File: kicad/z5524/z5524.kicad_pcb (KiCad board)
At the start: 4 copper layers, 80 x 80 mm, 203 parts, among them J1 Conn_01x01, J2 Conn_01x02, J3 Conn_02x20_Odd_Even, Q1 2N7002K, U1 TL074, U10 TL072, U11 NE5532, U12 TL074, U13 AS3364, U14 AD5328, U15 M24C02-WMN, U16 SSI2130, U17 DG442xY, U18 TL072, U19 LM311, U2 LM337L_TO92, U21 AD5328, U3 LM4040BIM3-2.5, U4 LM4040BIM3-4.1, U5 DG442xY, U6 TL072, U7 PCA9555D, U8 LM78L05_TO92, U9 AS3394

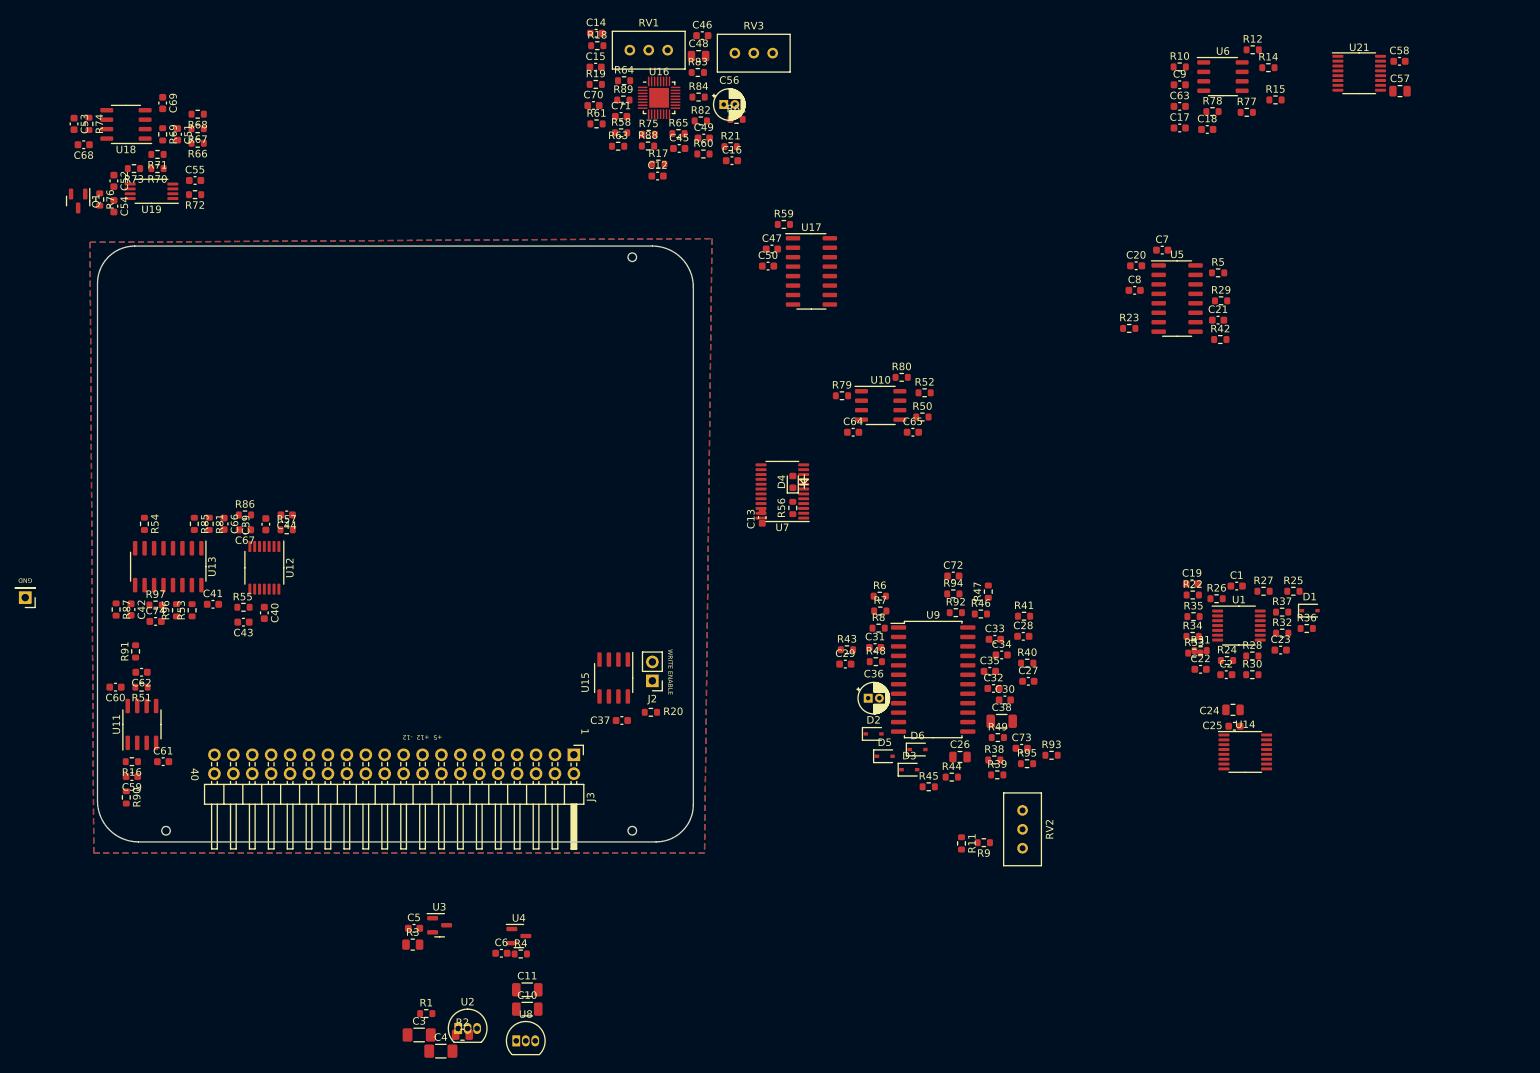
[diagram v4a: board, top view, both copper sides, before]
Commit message: further footprint mods; some placement
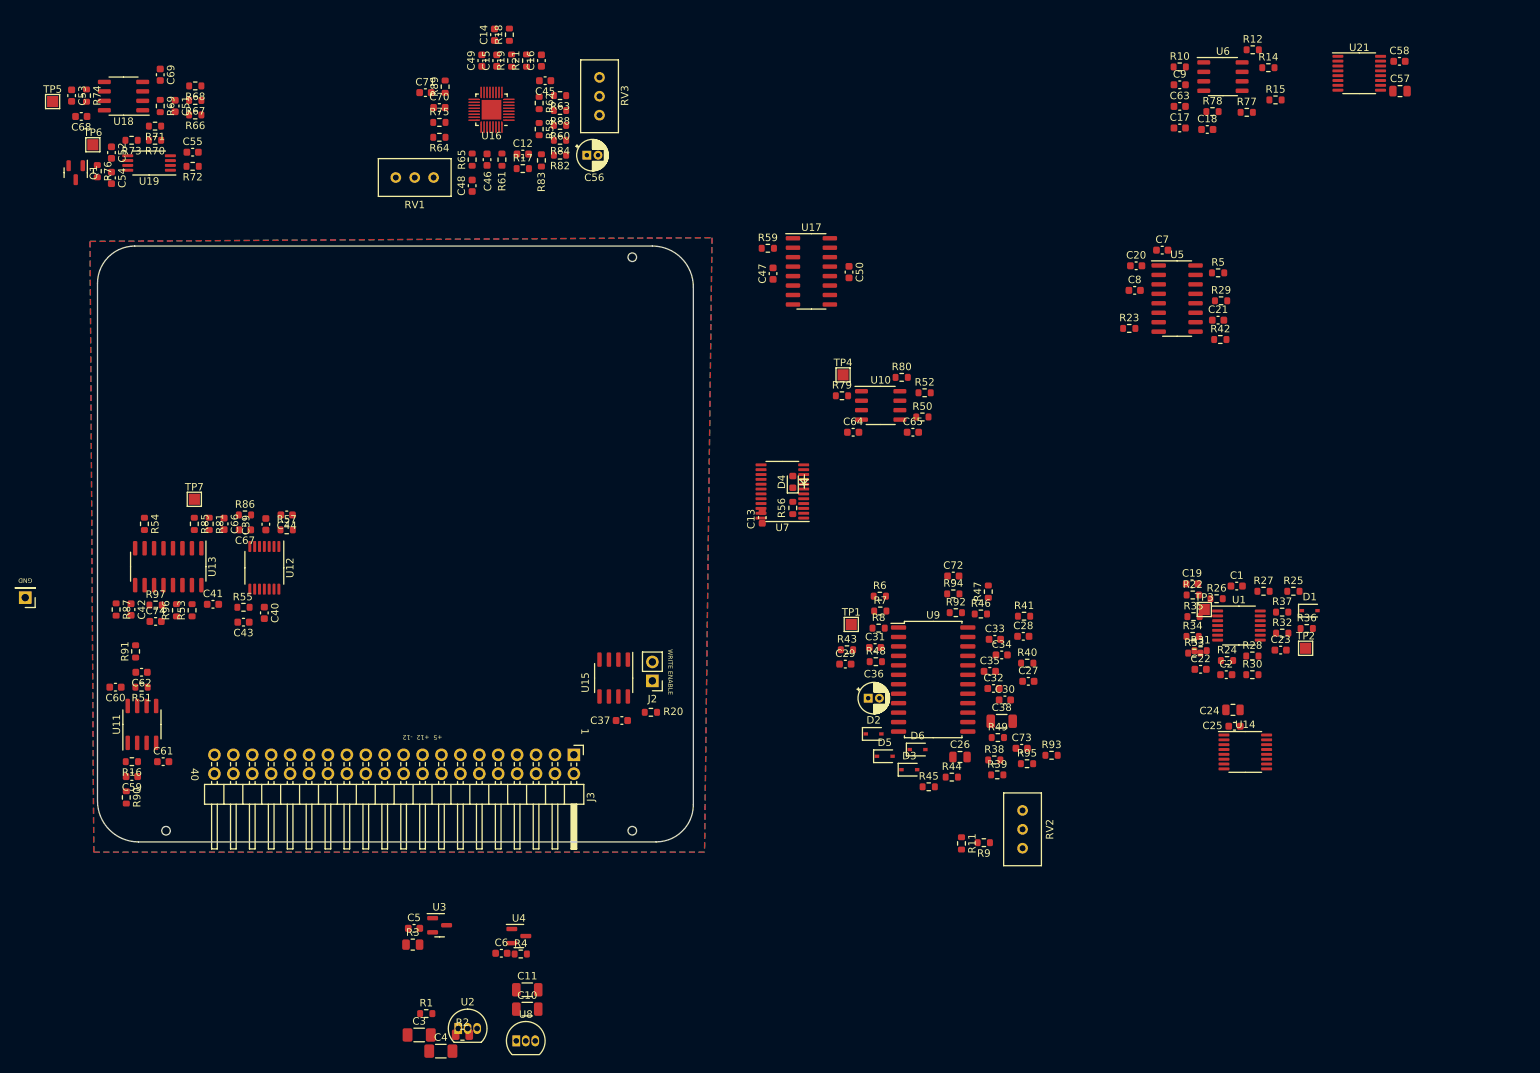
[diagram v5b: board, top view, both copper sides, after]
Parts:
- added TP1: TestPoint, TestPoint:TestPoint_Pad_1.5x1.5mm, F.Cu at (166.6, 75.7)
- added TP2: TestPoint, TestPoint:TestPoint_Pad_1.5x1.5mm, F.Cu at (227.6, 78.9)
- added TP3: TestPoint, TestPoint:TestPoint_Pad_1.5x1.5mm, F.Cu at (214.0, 73.7)
- added TP4: TestPoint, TestPoint:TestPoint_Pad_1.5x1.5mm, F.Cu at (165.5, 42.2)
- added TP5: TestPoint, TestPoint:TestPoint_Pad_1.5x1.5mm, F.Cu at (59.4, 5.50)
- added TP6: TestPoint, TestPoint:TestPoint_Pad_1.5x1.5mm, F.Cu at (64.8, 11.3)
- added TP7: TestPoint, TestPoint:TestPoint_Pad_1.5x1.5mm, F.Cu at (78.4, 58.9)
- C48: value 10u -> 10n; footprint Capacitor_SMD:C_0805_2012Metric -> Capacitor_SMD:C_0603_1608Metric
- C59: value 100p -> 68p
- R16: value 20k -> 39k
- moved RV1 40.3 mm to (105.5, 15.7), turned to 180 degrees
- moved C48 35.0 mm to (115.7, 16.8), turned to 90 degrees
- moved C46 33.4 mm to (117.7, 13.3), turned to -90 degrees
- moved C49 31.6 mm to (117.0, 0.00), turned to 90 degrees
- moved R21 29.7 mm to (123.0, 0.00), turned to 90 degrees
- moved C16 28.9 mm to (125.0, 0.00), turned to 90 degrees
- moved R75 28.1 mm to (111.3, 8.30)
- moved R65 27.9 mm to (115.7, 13.3), turned to -90 degrees
- moved R62 26.6 mm to (124.7, 5.70), turned to -90 degrees
- moved C71 26.5 mm to (109.4, 4.30)
- moved R64 25.9 mm to (111.3, 10.3), turned to 180 degrees
- moved R83 24.1 mm to (125.0, 13.4), turned to 90 degrees
- moved R89 24.0 mm to (112.1, 3.50), turned to 90 degrees
- moved RV3 23.5 mm to (132.8, 2.25), turned to 90 degrees
- moved U16 22.6 mm to (118.3, 6.60), turned to 180 degrees
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
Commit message: move blocks into board for eval
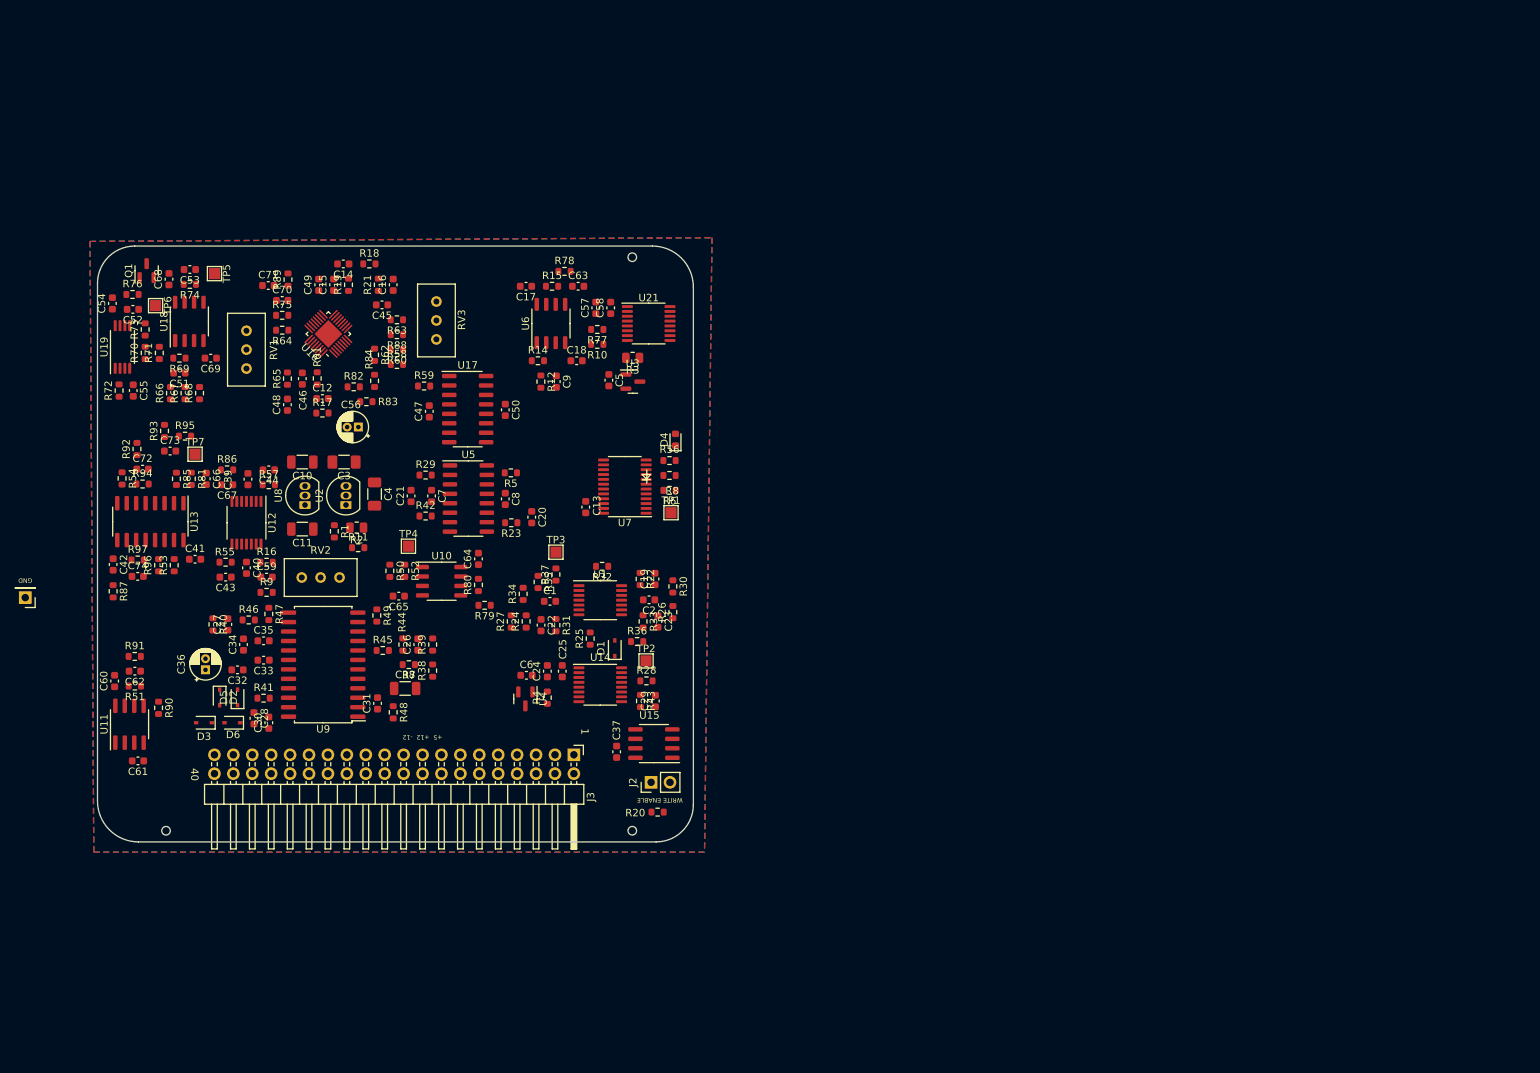
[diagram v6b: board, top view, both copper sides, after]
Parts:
- C24, C57: footprint Capacitor_SMD:C_0805_2012Metric -> Capacitor_SMD:C_0603_1608Metric
- C26: value 47n -> 33n; footprint Capacitor_SMD:C_0805_2012Metric -> Capacitor_SMD:C_0603_1608Metric
- R38, R39: value 4k7 -> 6k8
- moved R93 126.8 mm to (74.4, 49.7), turned to 90 degrees
- moved R95 121.3 mm to (77.2, 50.4)
- moved C73 121.1 mm to (75.2, 52.4)
- moved R92 112.1 mm to (70.7, 52.1), turned to 90 degrees
- moved C57 111.8 mm to (132.3, 33.2), turned to 90 degrees
- moved C58 111.0 mm to (134.3, 33.2), turned to 90 degrees
- moved C21 110.9 mm to (107.5, 58.5), turned to 90 degrees
- moved R94 109.8 mm to (71.5, 56.9)
- moved C72 109.8 mm to (71.5, 54.9)
- moved R40 109.4 mm to (80.9, 75.7), turned to -90 degrees
- moved R29 109.3 mm to (109.5, 55.6)
- moved R42 109.3 mm to (109.5, 61.1)
- moved C27 107.7 mm to (82.9, 75.7), turned to 90 degrees
- moved R14 105.7 mm to (124.5, 40.3)
- moved R12 105.4 mm to (124.9, 43.1), turned to -90 degrees
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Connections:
- net Net-(R49-Pad2) renamed /AS3394/VCO_3394
- net Net-(R79-Pad1) renamed /AS3394/SAWTOOTH_3394
- D1 pad 1: +5VA -> +5V
- U11 pad 1: /SSI2130_VCO -> Net-(U11-Pad1)
- U11 pad 2: /SSI2130/MIX_OUT -> Net-(U11-Pad1)
- U12 pad 13: Net-(U12-Pad13) -> /SSI2130/MIX_OUT
- U12 pad 14: Net-(U12-Pad13) -> /SSI2130_VCO
- U14 pad 12: /DAC 3394/FINAL_GAIN_DAC_CV -> /DAC 3394/VCO_DAC_CV
- U14 pad 13: /DAC 3394/SSI2130_MOD_DAC_CV -> /DAC 3394/VCF_DAC_CV
- U14 pad 4: /DAC 3394/VCO_DAC_CV -> /DAC 3394/FINAL_GAIN_DAC_CV
- U14 pad 7: /DAC 3394/VCF_DAC_CV -> /DAC 3394/SSI2130_MOD_DAC_CV
- U21 pad 4: /DAC 2130/EXP_PITCH_DAC -> /DAC 2130/PWM_DAC
- U21 pad 5: /DAC 2130/LINEAR_DAC -> /DAC 2130/SAW_MIX_DAC
- U21 pad 6: /DAC 2130/PWM_DAC -> /DAC 2130/LINEAR_DAC
- U21 pad 7: /DAC 2130/SAW_MIX_DAC -> /DAC 2130/EXP_PITCH_DAC
- U7 pad 13: unconnected-(U7-Pad13) -> /SOFTSYNC_2130_CTRL
- U7 pad 14: unconnected-(U7-Pad14) -> /PWM2130_MOD_CTRL
- U7 pad 15: unconnected-(U7-Pad15) -> /HARDSYNC_2130_CTRL
- U7 pad 16: unconnected-(U7-Pad16) -> /FM2130_MOD_CTRL
- U7 pad 17: /SOFTSYNC_2130_CTRL -> /VCO3394_EXP_MOD_CTRL
- U7 pad 18: /HARDSYNC_2130_CTRL -> /WAVESELECT_MOD_CTRL
- U7 pad 19: /FM2130_MOD_CTRL -> /PWM3394_MOD_CTRL
- U7 pad 20: /PWM2130_MOD_CTRL -> /VCF3394_MOD_CTRL
- U7 pad 4: /VCO3394_EXP_MOD_CTRL -> unconnected-(U7-Pad4)
- U7 pad 5: /VCF3394_MOD_CTRL -> unconnected-(U7-Pad5)
- U7 pad 6: /PWM3394_MOD_CTRL -> unconnected-(U7-Pad6)
- U7 pad 7: /WAVESELECT_MOD_CTRL -> unconnected-(U7-Pad7)
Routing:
- net GND: track 97.5 -> 76.1 mm
- net Net-(R64-Pad2): track 0.00 -> 12.3 mm
- net Net-(R88-Pad1): track 0.00 -> 9.17 mm
